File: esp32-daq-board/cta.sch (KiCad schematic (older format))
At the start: 34 parts, among them J1 Barrel_Jack_MountingPin, J2 Conn_01x15_Female, J3 Conn_01x15_Female, J5V1 Conn_01x03, U5V1 LM7805_TO220

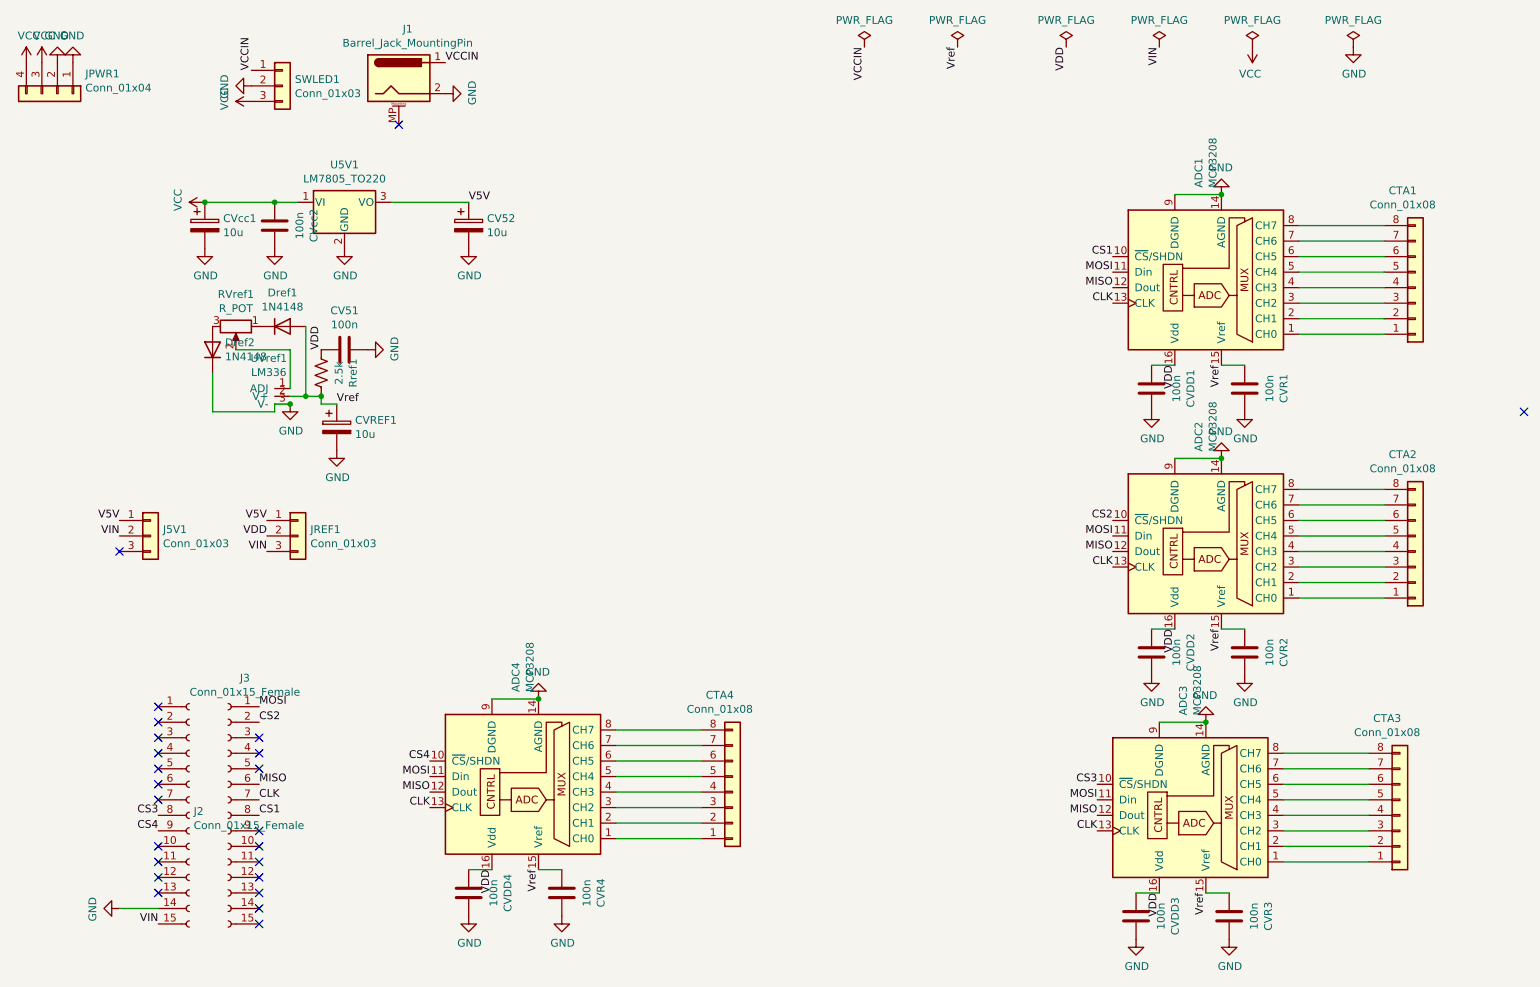
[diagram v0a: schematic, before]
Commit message: Major changes in the esp daq board.
Now the analog ground is given in a ninth wire for each board in the same flat cable.

Power supply will be from the ESP board.
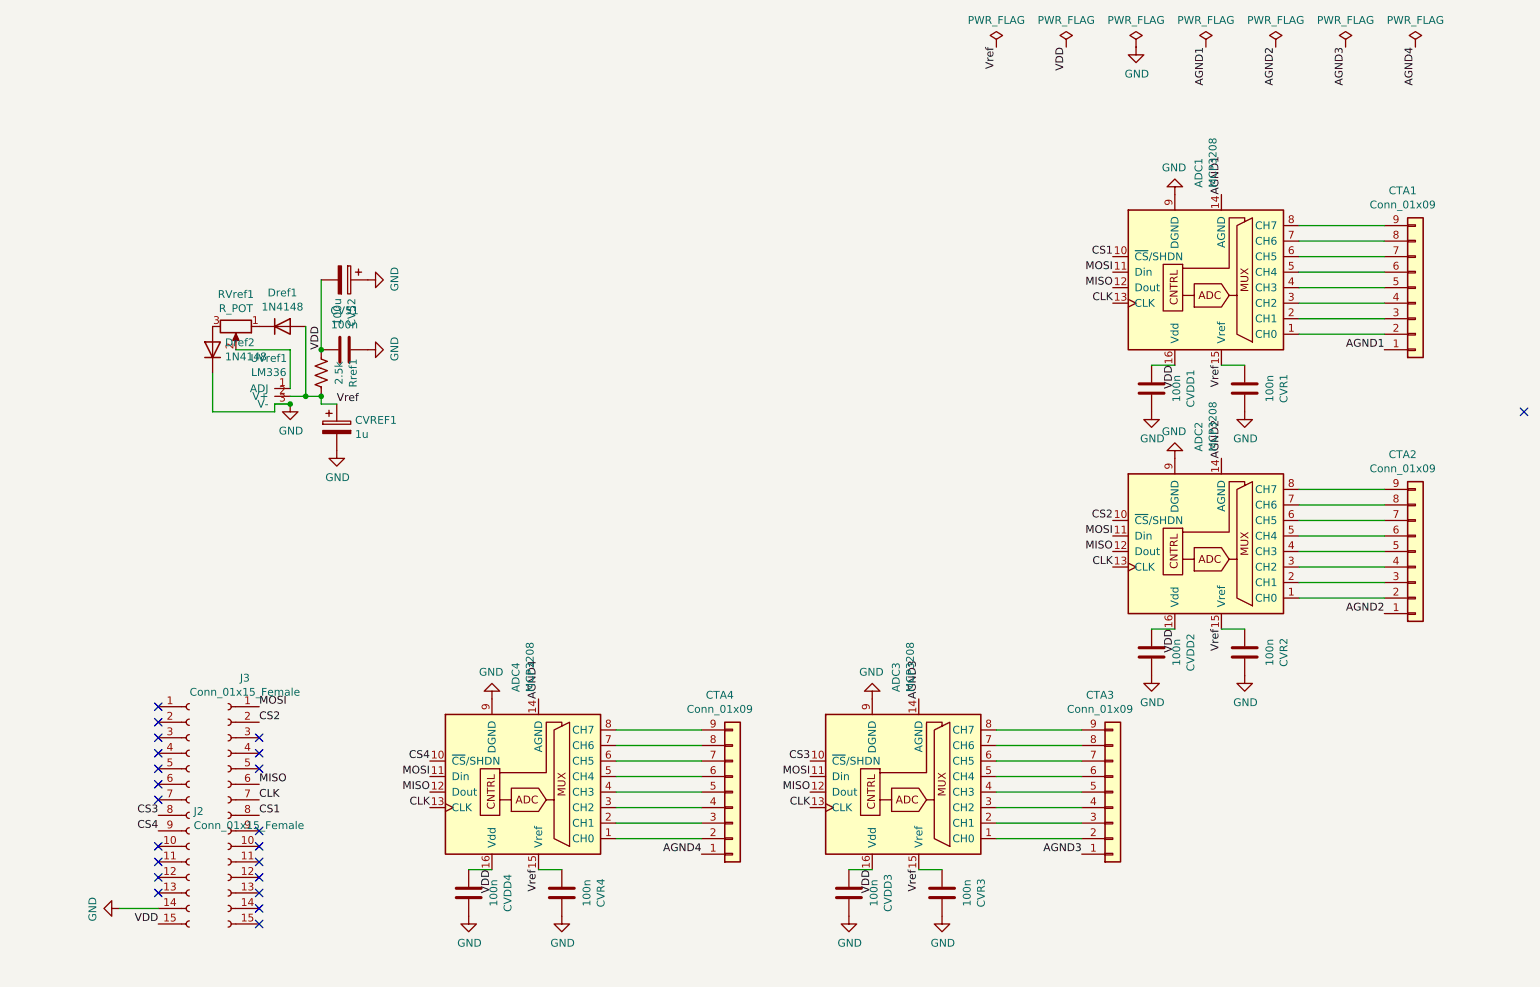
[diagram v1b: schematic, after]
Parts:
- removed CTA1, CTA2, CTA3, CTA4: Conn_01x08, Connector_PinHeader_2.54mm:PinHeader_1x08_P2.54mm_Vertical, symbol Connector_Generic:Conn_01x08
- removed CVcc1: 10u, Capacitor_THT:CP_Radial_D4.0mm_P2.00mm, symbol Device:CP
- removed CVcc2: 100n, Capacitor_THT:C_Rect_L7.2mm_W3.0mm_P5.00mm_FKS2_FKP2_MKS2_MKP2, symbol Device:C
- removed J1: Barrel_Jack_MountingPin, Connector_BarrelJack:BarrelJack_Horizontal, symbol Connector:Barrel_Jack_MountingPin
- removed J5V1, JREF1: Conn_01x03, Connector_PinHeader_2.54mm:PinHeader_1x03_P2.54mm_Vertical, symbol Connector_Generic:Conn_01x03
- removed JPWR1: Conn_01x04, TerminalBlock:TerminalBlock_bornier-4_P5.08mm, symbol Connector_Generic:Conn_01x04
- removed SWLED1: Conn_01x03, TerminalBlock:TerminalBlock_bornier-3_P5.08mm, symbol Connector_Generic:Conn_01x03
- removed U5V1: LM7805_TO220, Package_TO_SOT_THT:TO-220-3_Vertical, symbol Regulator_Linear:LM7805_TO220
- added CTA1, CTA2, CTA3, CTA4: Conn_01x09, Connector_PinHeader_2.54mm:PinHeader_1x09_P2.54mm_Vertical, symbol Connector_Generic:Conn_01x09
- CV52: value 10u -> 100u; footprint Capacitor_THT:CP_Radial_D4.0mm_P2.00mm -> Capacitor_THT:CP_Radial_D6.3mm_P2.50mm
- CVREF1: value 10u -> 1u
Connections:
- net V5V is gone; now on net GND: CV52.1
- net VIN is gone; now on net VDD: J2.15 (Pin_15)
- net GND: no longer ADC1.14 (AGND), ADC2.14 (AGND), ADC3.14 (AGND), ADC4.14 (AGND), CV52.2
- net VDD: now also CV52.2
- net at ADC1.1 (CH0): now also CTA1.2 (Pin_2)
- net at ADC1.2 (CH1): now also CTA1.3 (Pin_3)
- net at ADC1.3 (CH2): now also CTA1.4 (Pin_4)
- net at ADC1.4 (CH3): now also CTA1.5 (Pin_5)
- net at ADC1.5 (CH4): now also CTA1.6 (Pin_6)
- net at ADC1.6 (CH5): now also CTA1.7 (Pin_7)
- net at ADC1.7 (CH6): now also CTA1.8 (Pin_8)
- net at ADC1.8 (CH7): now also CTA1.9 (Pin_9)
- net at ADC2.1 (CH0): now also CTA2.2 (Pin_2)
- net at ADC2.2 (CH1): now also CTA2.3 (Pin_3)
- net at ADC2.3 (CH2): now also CTA2.4 (Pin_4)
- net at ADC2.4 (CH3): now also CTA2.5 (Pin_5)
- net at ADC2.5 (CH4): now also CTA2.6 (Pin_6)
- net at ADC2.6 (CH5): now also CTA2.7 (Pin_7)
- net at ADC2.7 (CH6): now also CTA2.8 (Pin_8)
- net at ADC2.8 (CH7): now also CTA2.9 (Pin_9)
- net at ADC3.1 (CH0): now also CTA3.2 (Pin_2)
- net at ADC3.2 (CH1): now also CTA3.3 (Pin_3)
- net at ADC3.3 (CH2): now also CTA3.4 (Pin_4)
- net at ADC3.4 (CH3): now also CTA3.5 (Pin_5)
- net at ADC3.5 (CH4): now also CTA3.6 (Pin_6)
- net at ADC3.6 (CH5): now also CTA3.7 (Pin_7)
- net at ADC3.7 (CH6): now also CTA3.8 (Pin_8)
- net at ADC3.8 (CH7): now also CTA3.9 (Pin_9)
- net at ADC4.1 (CH0): now also CTA4.2 (Pin_2)
- net at ADC4.2 (CH1): now also CTA4.3 (Pin_3)
- net at ADC4.3 (CH2): now also CTA4.4 (Pin_4)
- net at ADC4.4 (CH3): now also CTA4.5 (Pin_5)
- net at ADC4.5 (CH4): now also CTA4.6 (Pin_6)
- net at ADC4.6 (CH5): now also CTA4.7 (Pin_7)
- net at ADC4.7 (CH6): now also CTA4.8 (Pin_8)
- net at ADC4.8 (CH7): now also CTA4.9 (Pin_9)
- new net AGND1: ADC1.14 (AGND), CTA1.1 (Pin_1)
- new net AGND2: ADC2.14 (AGND), CTA2.1 (Pin_1)
- new net AGND3: ADC3.14 (AGND), CTA3.1 (Pin_1)
- new net AGND4: ADC4.14 (AGND), CTA4.1 (Pin_1)
- no-connect marks 24 -> 22
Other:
- moved on the sheet: ADC3, CVDD3, CVR3

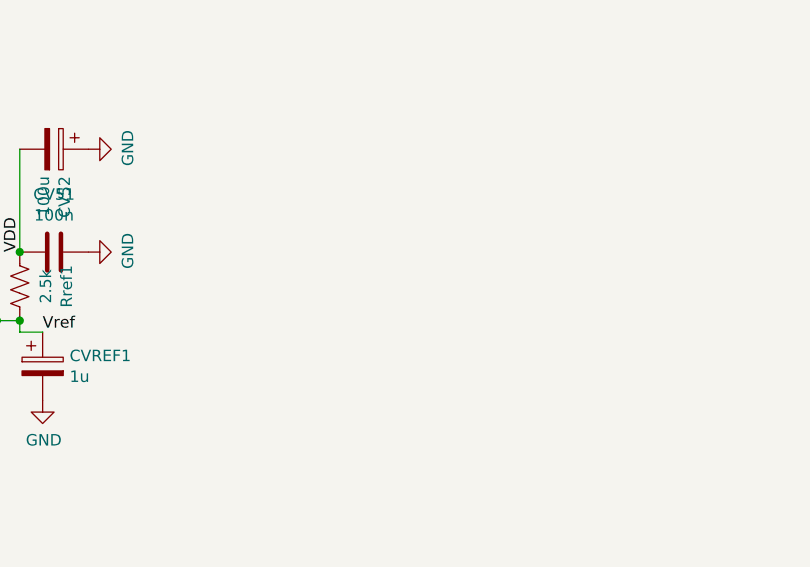
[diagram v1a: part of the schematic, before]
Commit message: Added a terminal block to esp32-daq-board
This terminal exposes the 5V supply, reference voltage and ground. This makes it easier to adjust the the reference voltage.
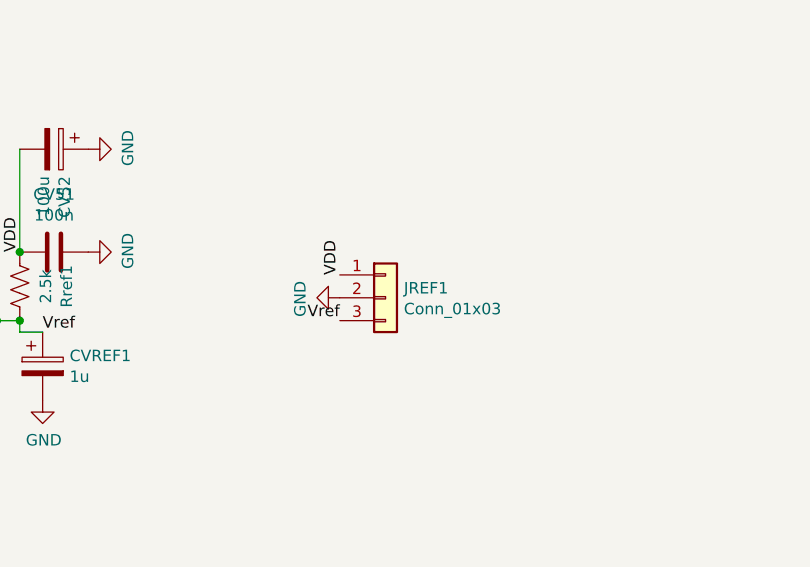
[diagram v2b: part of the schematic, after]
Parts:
- added JREF1: Conn_01x03, TerminalBlock:TerminalBlock_bornier-3_P5.08mm, symbol Connector_Generic:Conn_01x03
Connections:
- net GND: now also JREF1.2 (Pin_2)
- net VDD: now also JREF1.1 (Pin_1)
- net Vref: now also JREF1.3 (Pin_3)
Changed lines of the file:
@@
 	2950 2900 2950 2450
 Connection ~ 2950 2900
+$Comp
+L Connector_Generic:Conn_01x03 JREF1
+U 1 1 60BADDF4
+P 4550 3100
+F 0 "JREF1" H 4630 3142 50  0000 L CNN
+F 1 "Conn_01x03" H 4630 3051 50  0000 L CNN
+F 2 "TerminalBlock:TerminalBlock_bornier-3_P5.08mm" H 4550 3100 50  0001 C CNN
+F 3 "~" H 4550 3100 50  0001 C CNN
+	1    4550 3100
+	1    0    0    -1
+$EndComp
+$Comp
+L power:GND #PWR0102
+U 1 1 60BB09A8
+P 4350 3100
+F 0 "#PWR0102" H 4350 2850 50  0001 C CNN
+F 1 "GND" H 4355 2927 50  0000 C CNN
+F 2 "" H 4350 3100 50  0001 C CNN
+F 3 "" H 4350 3100 50  0001 C CNN
+	1    4350 3100
+	0    1    1    0
+$EndComp
+Text Label 4350 3200 2    50   ~ 0
+Vref
+Text Label 4350 3000 1    50   ~ 0
+VDD
 $EndSCHEMATC
